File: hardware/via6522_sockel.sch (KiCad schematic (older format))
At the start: 3 parts, among them P1 VIA_PIN_1-20, P2 DIL40, P3 VIA_PIN_21-40

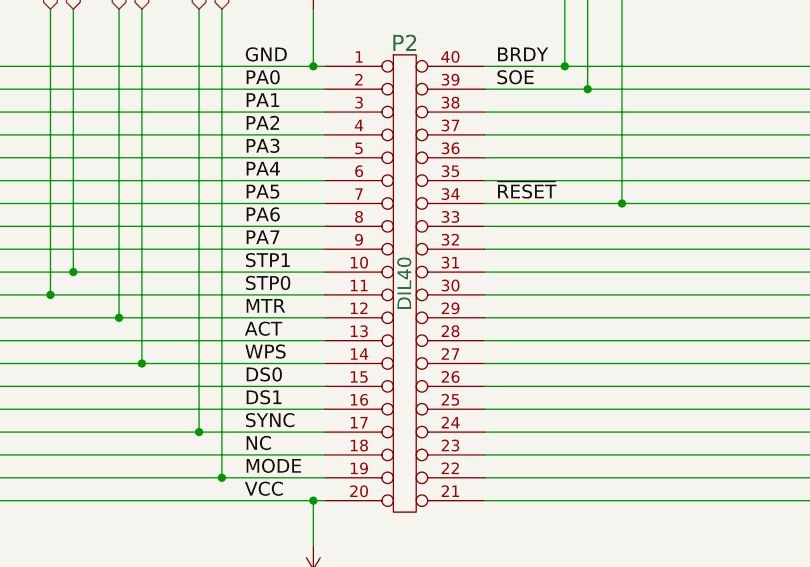
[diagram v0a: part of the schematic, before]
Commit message: - Anordnung aller Bauteile (Problem noch mit SD-Slot) - Erstes PCB Layout mit Freeroute - Autorouter.
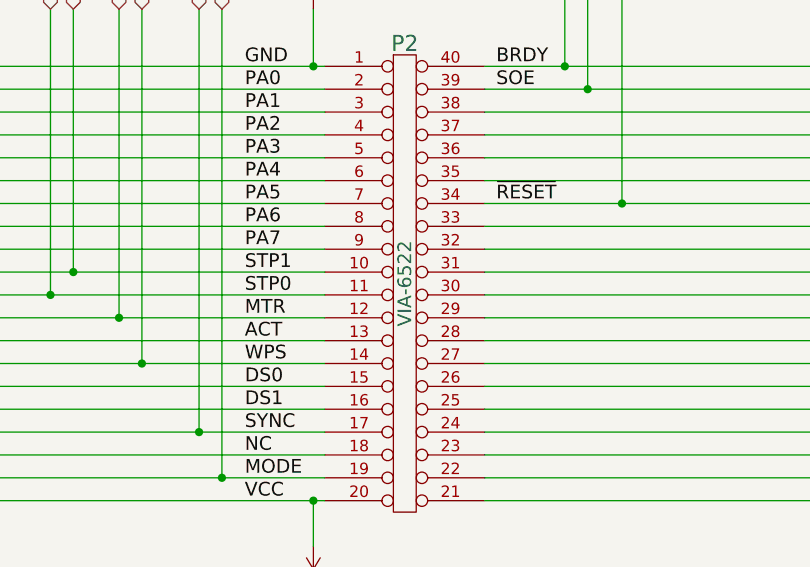
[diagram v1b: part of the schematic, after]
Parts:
- P2: value DIL40 -> VIA-6522
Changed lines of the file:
@@
 LIBS:w_transistor
 LIBS:w_vacuum
+LIBS:kattanek
 LIBS:1541-rebuild-cache
 EELAYER 25 0
@@
 Rev "1.3.3"
 Comp ""
-Comment1 "Erstellt: von: Thorsten Kattanek"
+Comment1 "Erstellt von: Thorsten Kattanek"
 Comment2 ""
 Comment3 ""
@@
 P 6400 3850
 F 0 "P2" H 6400 4900 70  0000 C CNN
-F 1 "DIL40" V 6400 3850 60  0000 C CNN
+F 1 "VIA-6522" V 6400 3850 60  0000 C CNN
 F 2 "w_pth_circuits:dil_40-600_socket" H 6400 3850 60  0001 C CNN
 F 3 "" H 6400 3850 60  0000 C CNN

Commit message: Hardware Projekt knovertiert von KiCad 4 -> KiCad 5 - Schaltplan angepasst - neues Detailfoto hinzugefügt - Footprints neu zugeordnet, somit ist auch wieder eine 3D Darstellung möglich - Readme.md angepasst
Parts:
- removed P2: VIA-6522, w_pth_circuits:dil_40-600_socket, symbol DIL40
- added IC2: VIA6522, Package_DIP:DIP-40_W15.24mm_Socket_LongPads, symbol floppy1541_tk:VIA6522
- P1: footprint Pin_Headers:Pin_Header_Straight_1x20_Pitch2.54mm -> Connector_PinHeader_2.54mm:PinHeader_1x20_P2.54mm_Vertical; symbol CONN_01X20 -> Connector_Generic:Conn_01x20
- P2: renamed from P3; footprint Pin_Headers:Pin_Header_Straight_1x20_Pitch2.54mm -> Connector_PinHeader_2.54mm:PinHeader_1x20_P2.54mm_Vertical; symbol CONN_01X20 -> Connector_Generic:Conn_01x20
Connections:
- net +5V: now also IC2.20 (VCC)
- net ACT: now also IC2.13 (PB3)
- net BRDY: now also IC2.40 (CA1)
- net DS0: now also IC2.15 (PB5)
- net DS1: now also IC2.16 (PB6)
- net GND: now also IC2.1 (VSS)
- net MTR: now also IC2.12 (PB2)
- net NC: now also IC2.18 (CB1)
- net OE: now also IC2.19 (CB2)
- net PA0: now also IC2.2 (PA0)
- net PA1: now also IC2.3 (PA1)
- net PA2: now also IC2.4 (PA2)
- net PA3: now also IC2.5 (PA3)
- net PA4: now also IC2.6 (PA4)
- net PA5: now also IC2.7 (PA5)
- net PA6: now also IC2.8 (PA6)
- net PA7: now also IC2.9 (PA7)
- net SOE: now also IC2.39 (CA2)
- net SPT0: now also IC2.11 (PB1)
- net STP1: now also IC2.10 (PB0)
- net SYNC: now also IC2.17 (PB7)
- net WPS: now also IC2.14 (PB4)
- net ~RESET: now also IC2.34 (~RESET)
- net at P2.1 (Pin_1): now also IC2.21 (~IRQ)
- net at P2.2 (Pin_2): now also IC2.22 (R/W)
- net at P2.3 (Pin_3): now also IC2.23 (~CS2)
- net at P2.4 (Pin_4): now also IC2.24 (CS1)
- net at P2.5 (Pin_5): now also IC2.25 (PHI2)
- net at P2.6 (Pin_6): now also IC2.26 (D7)
- net at P2.7 (Pin_7): now also IC2.27 (D6)
- net at P2.8 (Pin_8): now also IC2.28 (D5)
- net at P2.9 (Pin_9): now also IC2.29 (D4)
- net at P2.10 (Pin_10): now also IC2.30 (D3)
- net at P2.11 (Pin_11): now also IC2.31 (D2)
- net at P2.12 (Pin_12): now also IC2.32 (D1)
- net at P2.13 (Pin_13): now also IC2.33 (D0)
- net at P2.15 (Pin_15): now also IC2.35 (RS3)
- net at P2.16 (Pin_16): now also IC2.36 (RS2)
- net at P2.17 (Pin_17): now also IC2.37 (RS1)
- net at P2.18 (Pin_18): now also IC2.38 (RS0)
